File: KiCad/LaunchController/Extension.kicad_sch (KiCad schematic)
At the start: 3 parts, among them J7 CONN_STATUS_PANEL, J8 CONN_PANEL_BAORD_2, J9 CONN_PANEL_BAORD_1

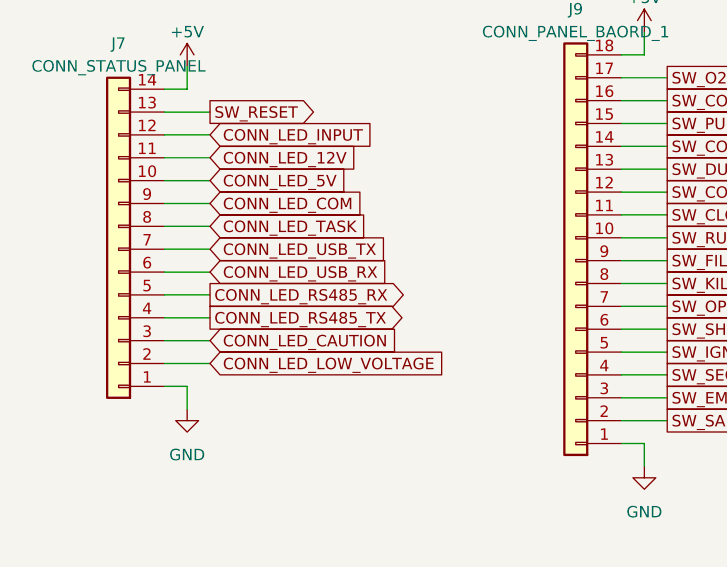
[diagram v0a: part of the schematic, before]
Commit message: USBのTX，RXを統合してACCESSに変更
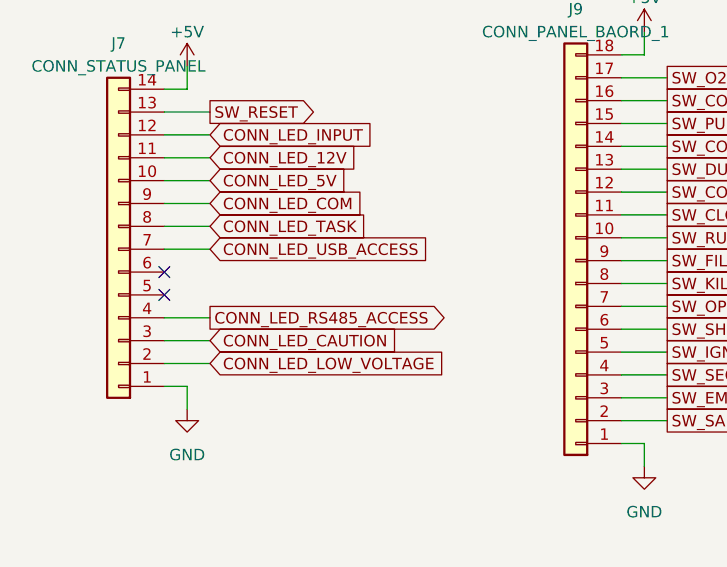
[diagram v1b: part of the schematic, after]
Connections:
- net CONN_LED_RS485_RX: no longer names the net of J7.5 (Pin_5)
- net CONN_LED_RS485_TX renamed CONN_LED_RS485_ACCESS
- net CONN_LED_USB_RX: no longer names the net of J7.6 (Pin_6)
- net CONN_LED_USB_TX renamed CONN_LED_USB_ACCESS
- no-connect marks 0 -> 2
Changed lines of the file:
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@@
 (kicad_sch (version 20230121) (generator eeschema)
   (paper "A4")
+  (no_connect (at 33.02 63.5))
+  (no_connect (at 33.02 66.04))
   (wire (pts (xy 83.82 67.31) (xy 88.9 67.31))
     (stroke (width 0) (type default))
@@
     (stroke (width 0) (type default))
   )
-  (wire (pts (xy 33.02 63.5) (xy 38.1 63.5))
-    (stroke (width 0) (type default))
-  )
   (wire (pts (xy 83.82 74.93) (xy 88.9 74.93))
     (stroke (width 0) (type default))
@@
     (stroke (width 0) (type default))
   )
-  (wire (pts (xy 33.02 66.04) (xy 38.1 66.04))
-    (stroke (width 0) (type default))
-  )
   (wire (pts (xy 33.02 68.58) (xy 38.1 68.58))
     (stroke (width 0) (type default))
@@
     )
   )
-  (global_label "CONN_LED_RS485_RX" (shape output) (at 38.1 66.04 0) (fields_autoplaced)
-    (effects (font (size 1.27 1.27)) (justify left))
-    (property "Intersheetrefs" "${INTERSHEET_REFS}" (at 61.2047 66.04 0)
-      (effects (font (size 1.27 1.27)) (justify left) hide)
-    )
-  )
   (global_label "CONN_LED_INPUT" (shape input) (at 38.1 48.26 0) (fields_autoplaced)
     (effects (font (size 1.27 1.27)) (justify left))
@@
     )
   )
-  (global_label "CONN_LED_USB_TX" (shape input) (at 38.1 60.96 0) (fields_autoplaced)
-    (effects (font (size 1.27 1.27)) (justify left))
-    (property "Intersheetrefs" "${INTERSHEET_REFS}" (at 58.6043 60.96 0)
+  (global_label "CONN_LED_USB_ACCESS" (shape input) (at 38.1 60.96 0) (fields_autoplaced)
+    (effects (font (size 1.27 1.27)) (justify left))
+    (property "Intersheetrefs" "${INTERSHEET_REFS}" (at 63.6238 60.96 0)
       (effects (font (size 1.27 1.27)) (justify left) hide)
     )
@@
     )
   )
-  (global_label "CONN_LED_USB_RX" (shape input) (at 38.1 63.5 0) (fields_autoplaced)
-    (effects (font (size 1.27 1.27)) (justify left))
-    (property "Intersheetrefs" "${INTERSHEET_REFS}" (at 58.9067 63.5 0)
-      (effects (font (size 1.27 1.27)) (justify left) hide)
-    )
-  )
   (global_label "CONN_LED_TASK" (shape input) (at 38.1 58.42 0) (fields_autoplaced)
     (effects (font (size 1.27 1.27)) (justify left))
@@
     )
   )
-  (global_label "CONN_LED_RS485_TX" (shape output) (at 38.1 68.58 0) (fields_autoplaced)
-    (effects (font (size 1.27 1.27)) (justify left))
-    (property "Intersheetrefs" "${INTERSHEET_REFS}" (at 60.9023 68.58 0)
-      (effects (font (size 1.27 1.27)) (justify left) hide)
-    )
+  (global_label "CONN_LED_RS485_ACCESS" (shape output) (at 38.1 68.58 0) (fields_autoplaced)
+    (effects (font (size 1.27 1.27)) (justify left))
+    (property "Intersheetrefs" "${INTERSHEET_REFS}" (at 65.9218 68.58 0)
+      (effects (font (size 1.27 1.27)) (justify left) hide)
+    )

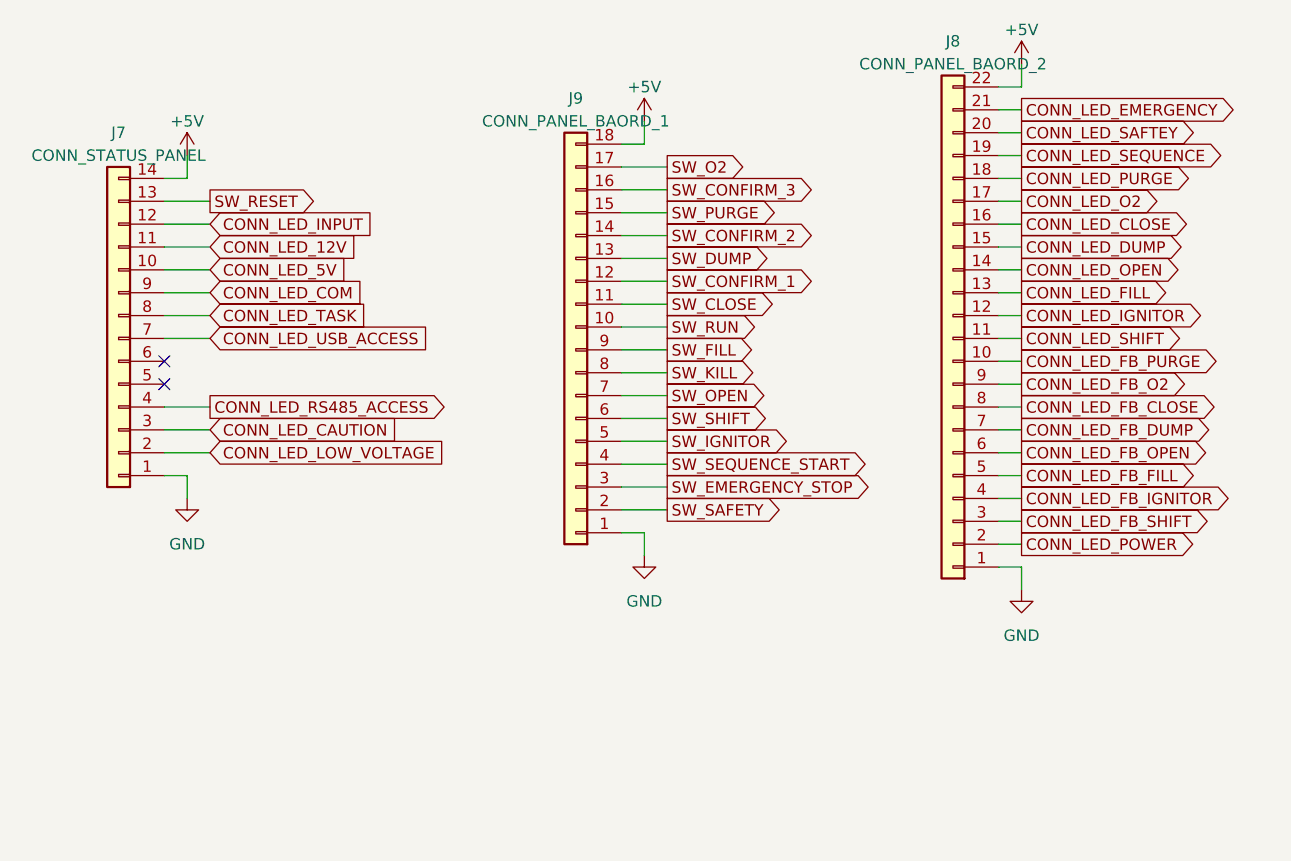
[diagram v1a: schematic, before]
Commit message: 充填確認スイッチ用のコネクタを別に用意
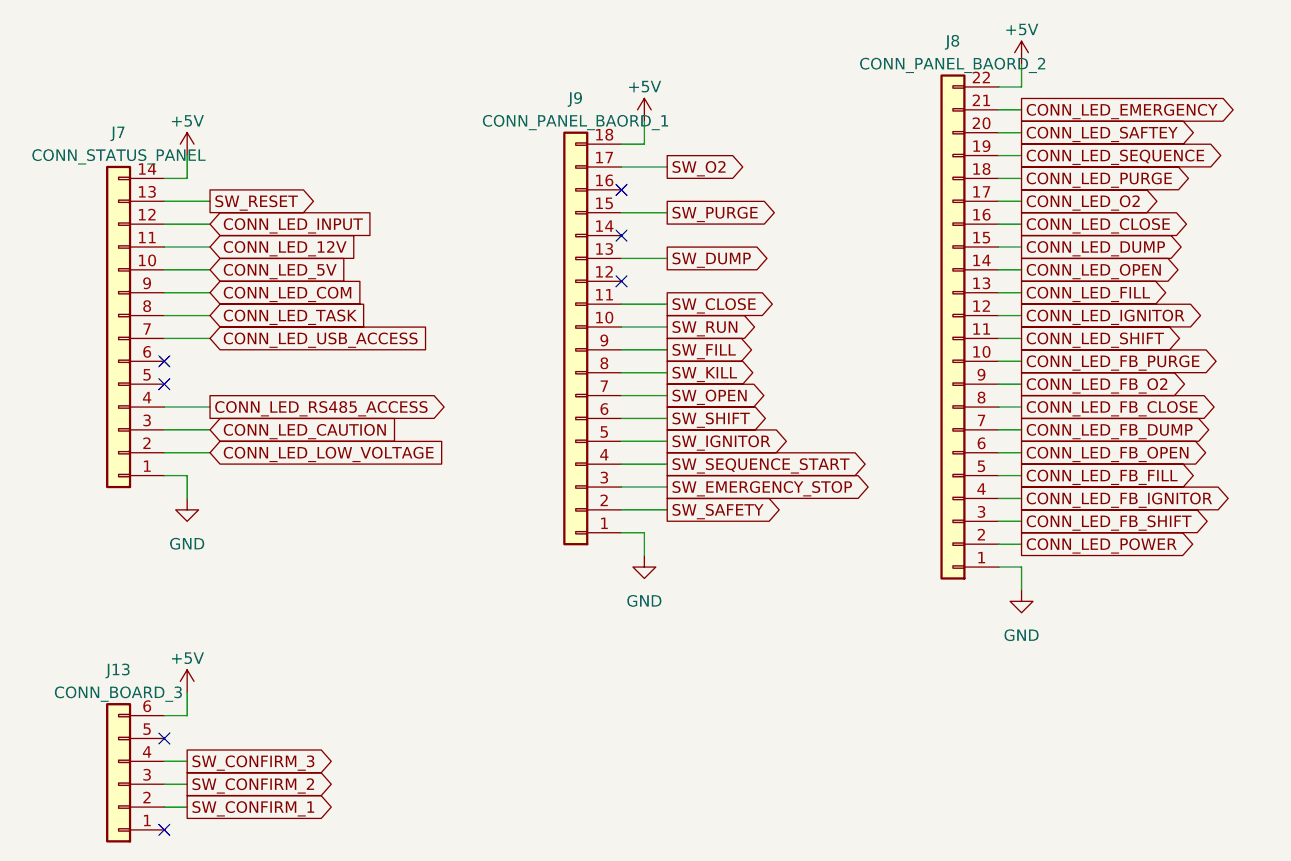
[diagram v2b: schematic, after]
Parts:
- added J13: CONN_BOARD_3, TSRP_Connector_Hirose:DF51A-6DP-2DSA, symbol Connector_Generic:Conn_01x06
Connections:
- net +5V: now also J13.6 (Pin_6)
- net SW_CONFIRM_1: now also J13.2 (Pin_2); no longer J9.12 (Pin_12)
- net SW_CONFIRM_2: now also J13.3 (Pin_3); no longer J9.14 (Pin_14)
- net SW_CONFIRM_3: now also J13.4 (Pin_4); no longer J9.16 (Pin_16)
- no-connect marks 2 -> 7
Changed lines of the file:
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@@
 (kicad_sch (version 20230121) (generator eeschema)
   (paper "A4")
+  (no_connect (at 83.82 49.53))
   (no_connect (at 33.02 63.5))
+  (no_connect (at 83.82 54.61))
+  (no_connect (at 33.02 115.57))
+  (no_connect (at 33.02 105.41))
+  (no_connect (at 83.82 44.45))
   (no_connect (at 33.02 66.04))
   (wire (pts (xy 83.82 67.31) (xy 88.9 67.31))
@@
     (stroke (width 0) (type default))
   )
-  (wire (pts (xy 83.82 44.45) (xy 88.9 44.45))
-    (stroke (width 0) (type default))
-  )
   (wire (pts (xy 83.82 64.77) (xy 88.9 64.77))
     (stroke (width 0) (type default))
@@
     (stroke (width 0) (type default))
   )
+  (wire (pts (xy 33.02 110.49) (xy 35.56 110.49))
+    (stroke (width 0) (type default))
+  )
   (wire (pts (xy 125.73 60.96) (xy 128.27 60.96))
     (stroke (width 0) (type default))
@@
     (stroke (width 0) (type default))
   )
-  (wire (pts (xy 83.82 54.61) (xy 88.9 54.61))
+  (wire (pts (xy 33.02 107.95) (xy 35.56 107.95))
     (stroke (width 0) (type default))
   )
@@
     (stroke (width 0) (type default))
   )
-  (wire (pts (xy 83.82 49.53) (xy 88.9 49.53))
-    (stroke (width 0) (type default))
-  )
   (wire (pts (xy 125.73 38.1) (xy 128.27 38.1))
     (stroke (width 0) (type default))
@@
     (stroke (width 0) (type default))
   )
+  (wire (pts (xy 35.56 102.87) (xy 33.02 102.87))
+    (stroke (width 0) (type default))
+  )
   (wire (pts (xy 33.02 68.58) (xy 38.1 68.58))
     (stroke (width 0) (type default))
@@
     (stroke (width 0) (type default))
   )
+  (wire (pts (xy 33.02 113.03) (xy 35.56 113.03))
+    (stroke (width 0) (type default))
+  )
   (wire (pts (xy 83.82 69.85) (xy 88.9 69.85))
     (stroke (width 0) (type default))
@@
     (stroke (width 0) (type default))
   )
+  (wire (pts (xy 35.56 100.33) (xy 35.56 102.87))
+    (stroke (width 0) (type default))
+  )
   (wire (pts (xy 83.82 52.07) (xy 88.9 52.07))
     (stroke (width 0) (type default))
@@
     )
   )
-  (global_label "SW_CONFIRM_1" (shape output) (at 88.9 54.61 0) (fields_autoplaced)
-    (effects (font (size 1.27 1.27)) (justify left))
-    (property "Intersheetrefs" "${INTERSHEET_REFS}" (at 105.9572 54.61 0)
-      (effects (font (size 1.27 1.27)) (justify left) hide)
-    )
-  )
   (global_label "CONN_LED_SEQUENCE" (shape output) (at 128.27 40.64 0) (fields_autoplaced)
     (effects (font (size 1.27 1.27)) (justify left))
@@
     )
   )
-  (global_label "SW_CONFIRM_3" (shape output) (at 88.9 44.45 0) (fields_autoplaced)
-    (effects (font (size 1.27 1.27)) (justify left))
-    (property "Intersheetrefs" "${INTERSHEET_REFS}" (at 105.9572 44.45 0)
-      (effects (font (size 1.27 1.27)) (justify left) hide)
-    )
-  )
   (global_label "CONN_LED_EMERGENCY" (shape output) (at 128.27 35.56 0) (fields_autoplaced)
     (effects (font (size 1.27 1.27)) (justify left))
@@
     )
   )
+  (global_label "SW_CONFIRM_1" (shape output) (at 35.56 113.03 0) (fields_autoplaced)
+    (effects (font (size 1.27 1.27)) (justify left))
+    (property "Intersheetrefs" "${INTERSHEET_REFS}" (at 52.6172 113.03 0)
+      (effects (font (size 1.27 1.27)) (justify left) hide)
+    )
+  )
   (global_label "SW_O2" (shape output) (at 88.9 41.91 0) (fields_autoplaced)
     (effects (font (size 1.27 1.27)) (justify left))
@@
     )
   )
+  (global_label "SW_CONFIRM_3" (shape output) (at 35.56 107.95 0) (fields_autoplaced)
+    (effects (font (size 1.27 1.27)) (justify left))
+    (property "Intersheetrefs" "${INTERSHEET_REFS}" (at 52.6172 107.95 0)
+      (effects (font (size 1.27 1.27)) (justify left) hide)
+    )
+  )
   (global_label "SW_OPEN" (shape output) (at 88.9 67.31 0) (fields_autoplaced)
     (effects (font (size 1.27 1.27)) (justify left))
@@
     )
   )
+  (global_label "SW_CONFIRM_2" (shape output) (at 35.56 110.49 0) (fields_autoplaced)
+    (effects (font (size 1.27 1.27)) (justify left))
+    (property "Intersheetrefs" "${INTERSHEET_REFS}" (at 52.6172 110.49 0)
+      (effects (font (size 1.27 1.27)) (justify left) hide)
+    )
+  )
   (global_label "CONN_LED_IGNITOR" (shape output) (at 128.27 58.42 0) (fields_autoplaced)
     (effects (font (size 1.27 1.27)) (justify left))
@@
     (effects (font (size 1.27 1.27)) (justify left))
     (property "Intersheetrefs" "${INTERSHEET_REFS}" (at 147.6858 66.04 0)
-      (effects (font (size 1.27 1.27)) (justify left) hide)
-    )
-  )
-  (global_label "SW_CONFIRM_2" (shape output) (at 88.9 49.53 0) (fields_autoplaced)
-    (effects (font (size 1.27 1.27)) (justify left))
-    (property "Intersheetrefs" "${INTERSHEET_REFS}" (at 105.9572 49.53 0)
       (effects (font (size 1.27 1.27)) (justify left) hide)
     )
@@
         )
       )
+    )
+  )
+  (symbol (lib_id "power:+5V") (at 35.56 100.33 0) (unit 1)
+    (in_bom yes) (on_board yes) (dnp no) (fields_autoplaced)
+    (property "Reference" "#PWR046" (at 35.56 104.14 0)
+      (effects (font (size 1.27 1.27)) hide)
+    )
+    (property "Value" "+5V" (at 35.56 96.52 0)
+      (effects (font (size 1.27 1.27)))
+    )
+    (property "Footprint" "" (at 35.56 100.33 0)
+      (effects (font (size 1.27 1.27)) hide)
+    )
+    (property "Datasheet" "" (at 35.56 100.33 0)
+      (effects (font (size 1.27 1.27)) hide)
+    )
+    (pin "1")
+    (instances
+      (project "LaunchController"
+        (path "/628d040b-43bf-4733-804f-091644a90124"
+          (reference "#PWR046") (unit 1)
+        )
+        (path "/628d040b-43bf-4733-804f-091644a90124/7294b7f8-79a7-4ea3-8687-92a673d94882"
+          (reference "#PWR068") (unit 1)
+        )
+      )
+    )
+  )
+  (symbol (lib_id "Connector_Generic:Conn_01x06") (at 27.94 110.49 180) (unit 1)
+    (in_bom yes) (on_board yes) (dnp no) (fields_autoplaced)
+    (property "Reference" "J13" (at 27.94 97.79 0)
+      (effects (font (size 1.27 1.27)))
+    )
+    (property "Value" "CONN_BOARD_3" (at 27.94 100.33 0)
+      (effects (font (size 1.27 1.27)))
+    )
+    (property "Footprint" "TSRP_Connector_Hirose:DF51A-6DP-2DSA" (at 27.94 110.49 0)
+      (effects (font (size 1.27 1.27)) hide)
+    )
+    (property "Datasheet" "~" (at 27.94 110.49 0)
+      (effects (font (size 1.27 1.27)) hide)
+    )
+    (pin "1")
+    (pin "2")
+    (pin "3")
+    (pin "4")
+    (pin "5")
+    (pin "6")
+    (instances
+      (project "LaunchController"
+        (path "/628d040b-43bf-4733-804f-091644a90124"
+          (reference "J13") (unit 1)
+        )
+        (path "/628d040b-43bf-4733-804f-091644a90124/7294b7f8-79a7-4ea3-8687-92a673d94882"
+          (reference "J14") (unit 1)
+        )
+      )

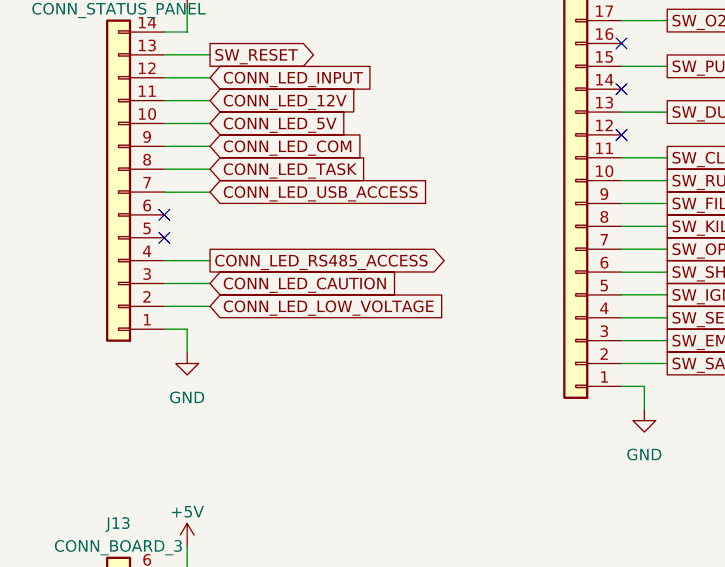
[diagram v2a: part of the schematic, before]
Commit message: CAUTIONをERRORに名称変更
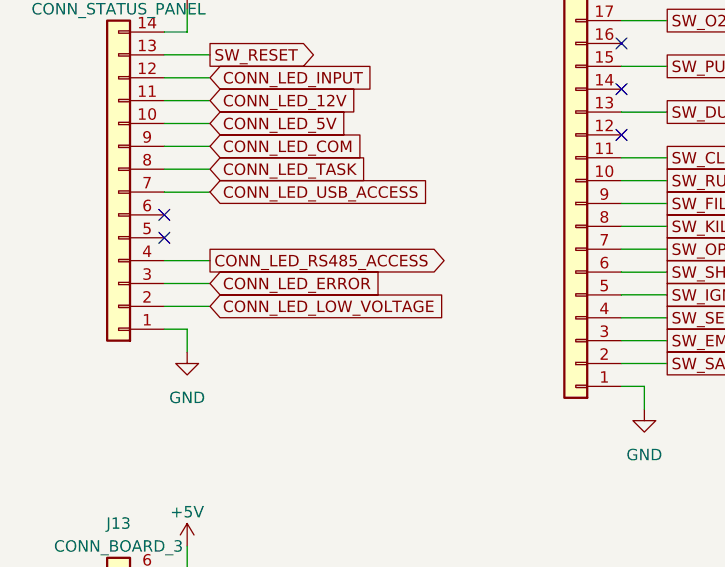
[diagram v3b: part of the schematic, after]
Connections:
- net CONN_LED_CAUTION renamed CONN_LED_ERROR
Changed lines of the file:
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@@
     )
   )
-  (global_label "CONN_LED_CAUTION" (shape input) (at 38.1 71.12 0) (fields_autoplaced)
+  (global_label "CONN_LED_ERROR" (shape input) (at 38.1 71.12 0) (fields_autoplaced)
     (effects (font (size 1.27 1.27)) (justify left))
-    (property "Intersheetrefs" "${INTERSHEET_REFS}" (at 59.5721 71.12 0)
+    (property "Intersheetrefs" "${INTERSHEET_REFS}" (at 57.9391 71.12 0)
       (effects (font (size 1.27 1.27)) (justify left) hide)
     )

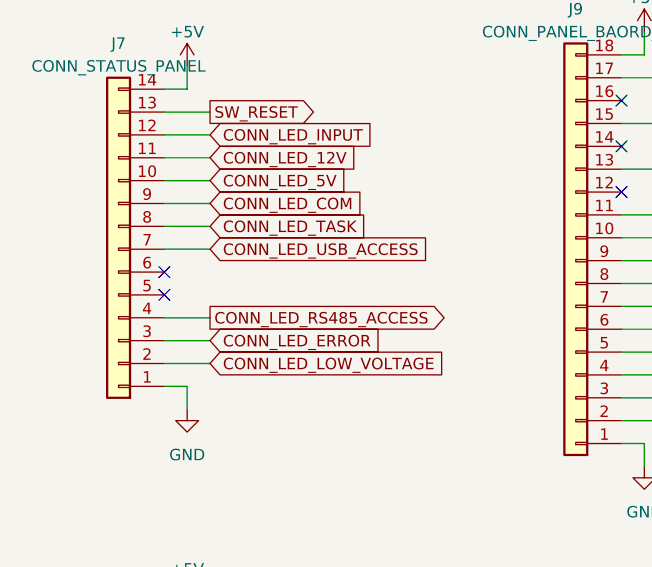
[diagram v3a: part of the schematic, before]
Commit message: 7セグ用コネクタを6Pから14Pの空いているピンに押し込んだ
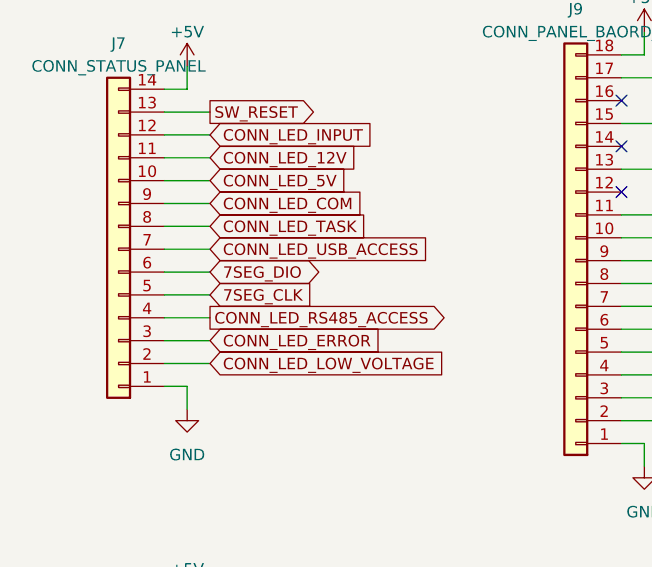
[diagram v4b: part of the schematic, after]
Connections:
- net 7SEG_CLK: now reaches J7.5 (Pin_5)
- net 7SEG_DIO: now reaches J7.6 (Pin_6)
- no-connect marks 7 -> 5
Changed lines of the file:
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@@
   (paper "A4")
   (no_connect (at 83.82 49.53))
-  (no_connect (at 33.02 63.5))
   (no_connect (at 83.82 54.61))
   (no_connect (at 33.02 115.57))
   (no_connect (at 33.02 105.41))
   (no_connect (at 83.82 44.45))
-  (no_connect (at 33.02 66.04))
   (wire (pts (xy 83.82 67.31) (xy 88.9 67.31))
     (stroke (width 0) (type default))
@@
     (stroke (width 0) (type default))
   )
+  (wire (pts (xy 33.02 63.5) (xy 38.1 63.5))
+    (stroke (width 0) (type default))
+  )
   (wire (pts (xy 35.56 102.87) (xy 33.02 102.87))
     (stroke (width 0) (type default))
@@
     (stroke (width 0) (type default))
   )
+  (wire (pts (xy 33.02 66.04) (xy 38.1 66.04))
+    (stroke (width 0) (type default))
+  )
   (wire (pts (xy 125.73 76.2) (xy 128.27 76.2))
     (stroke (width 0) (type default))
   )
+  (global_label "7SEG_CLK" (shape input) (at 38.1 66.04 0) (fields_autoplaced)
+    (effects (font (size 1.27 1.27)) (justify left))
+    (property "Intersheetrefs" "${INTERSHEET_REFS}" (at 50.3795 66.04 0)
+      (effects (font (size 1.27 1.27)) (justify left) hide)
+    )
+  )
   (global_label "SW_EMERGENCY_STOP" (shape output) (at 88.9 77.47 0) (fields_autoplaced)
     (effects (font (size 1.27 1.27)) (justify left))
@@
       (effects (font (size 1.27 1.27)) (justify left) hide)
     )
+  )
+  (global_label "7SEG_DIO" (shape bidirectional) (at 38.1 63.5 0) (fields_autoplaced)
+    (effects (font (size 1.27 1.27)) (justify left))
+    (property "Intersheetrefs" "${INTERSHEET_REFS}" (at 51.128 63.5 0)
+      (effects (font (size 1.27 1.27)) (justify left) hide)
+    )

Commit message: KiCad9.0に対応
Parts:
- renumbered J13 to J14
